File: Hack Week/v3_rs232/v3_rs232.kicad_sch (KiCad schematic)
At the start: 3 parts, among them J1 DE9_Socket, J2 Conn_01x04_Socket, U1 MAX3232

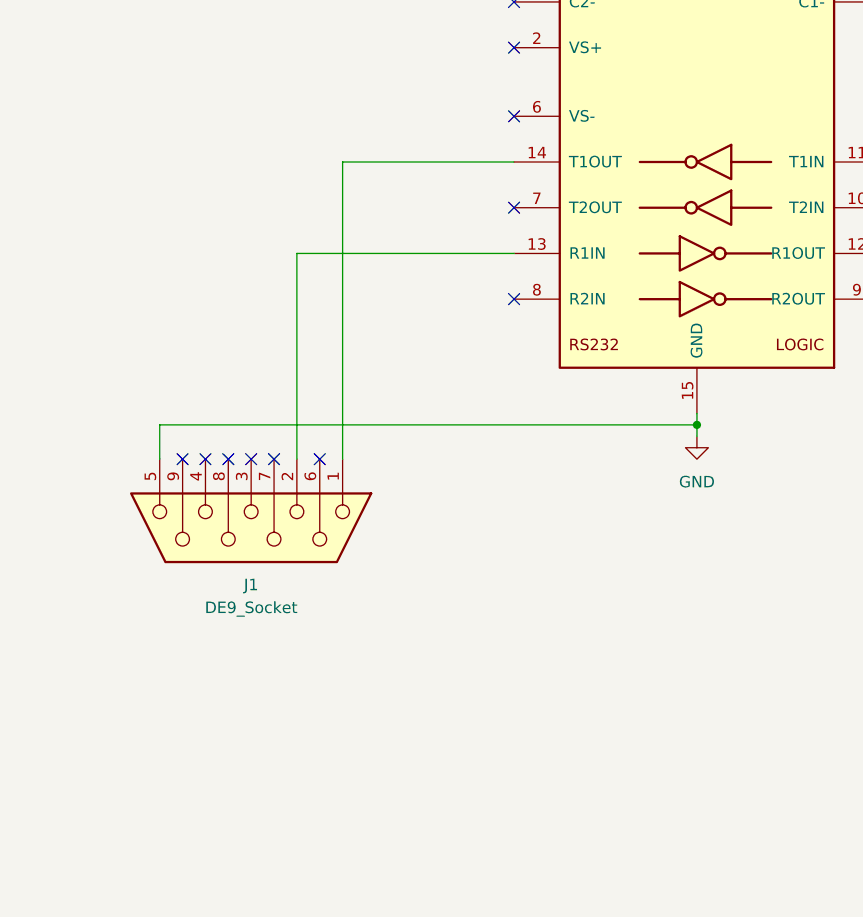
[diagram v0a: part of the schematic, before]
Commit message: changed DB9 connectors + added RS485
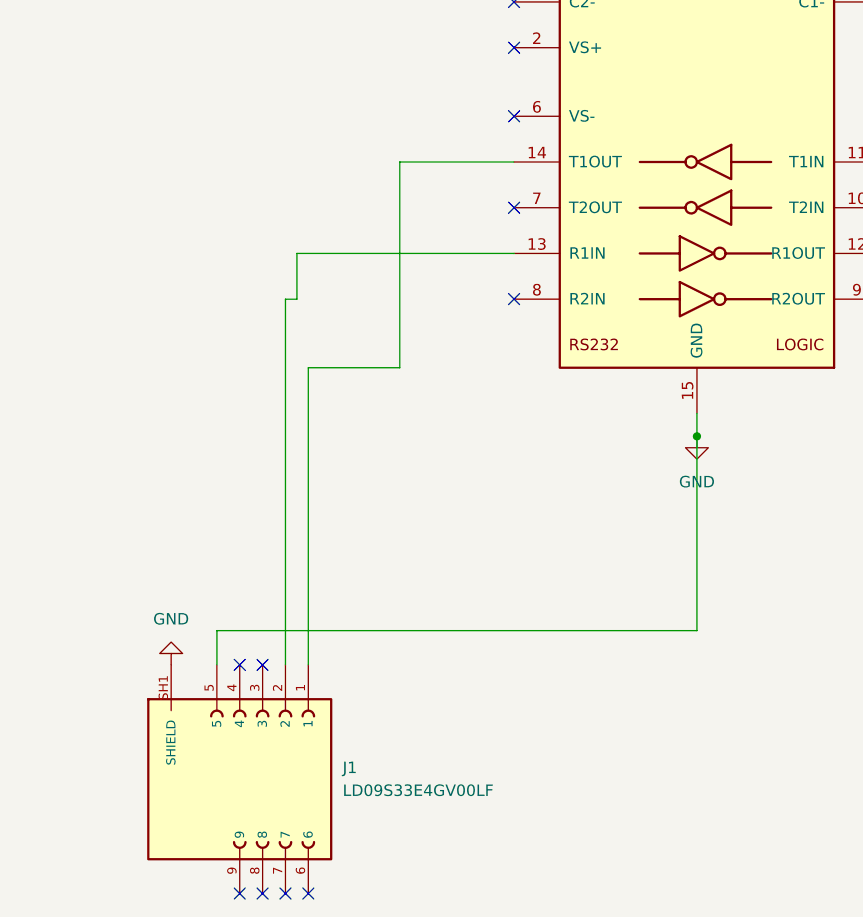
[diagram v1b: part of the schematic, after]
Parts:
- removed J1: DE9_Socket, Connector_Dsub:DSUB-9_Socket_EdgeMount_P2.77mm, symbol Connector:DE9_Socket
- added J1: LD09S33E4GV00LF, Connector_Pin:AMPHENOL_LD09S33E4GV00LF, symbol LD09S33E4GV00LF:LD09S33E4GV00LF
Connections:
- net GND: now also J1.5, J1.SH1 (SHIELD), J1.SH2 (SHIELD)
- net at U1.13 (R1IN): now also J1.2
- net at U1.14 (T1OUT): now also J1.1
